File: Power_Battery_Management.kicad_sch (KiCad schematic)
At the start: 11 parts, among them J501 S2B-PH-SM4-TB, Q501 CSD85302L, U501 BQ29737, U502 MCP73831T-2ACI/MC

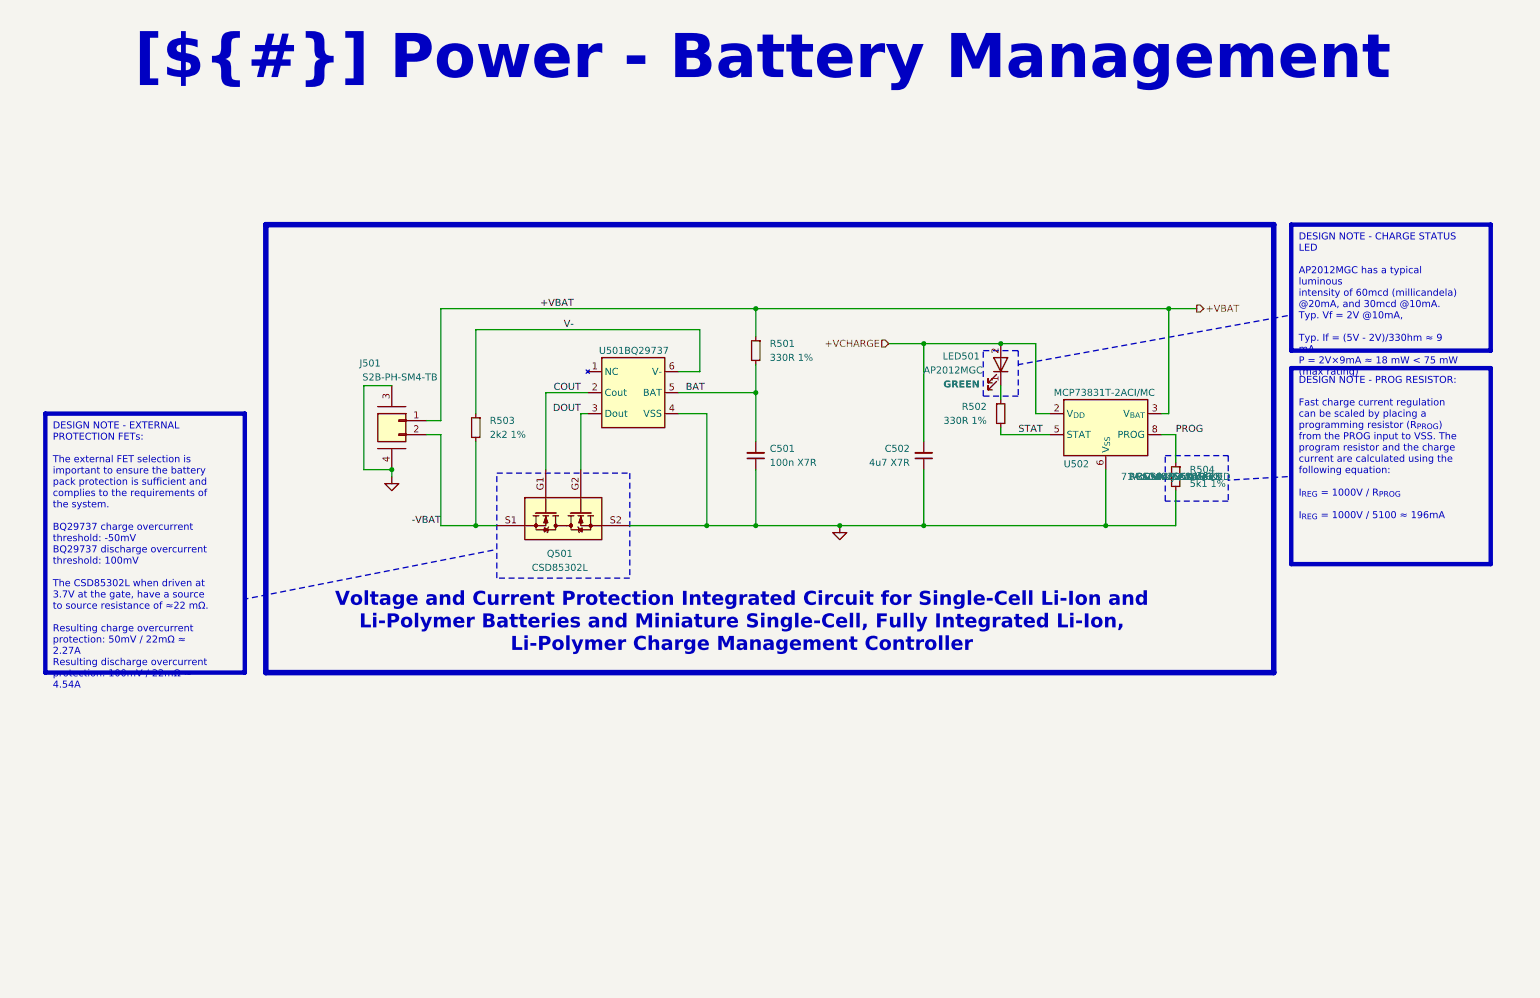
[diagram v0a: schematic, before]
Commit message: Added footprints, images, almost finished all èages except for the MCU
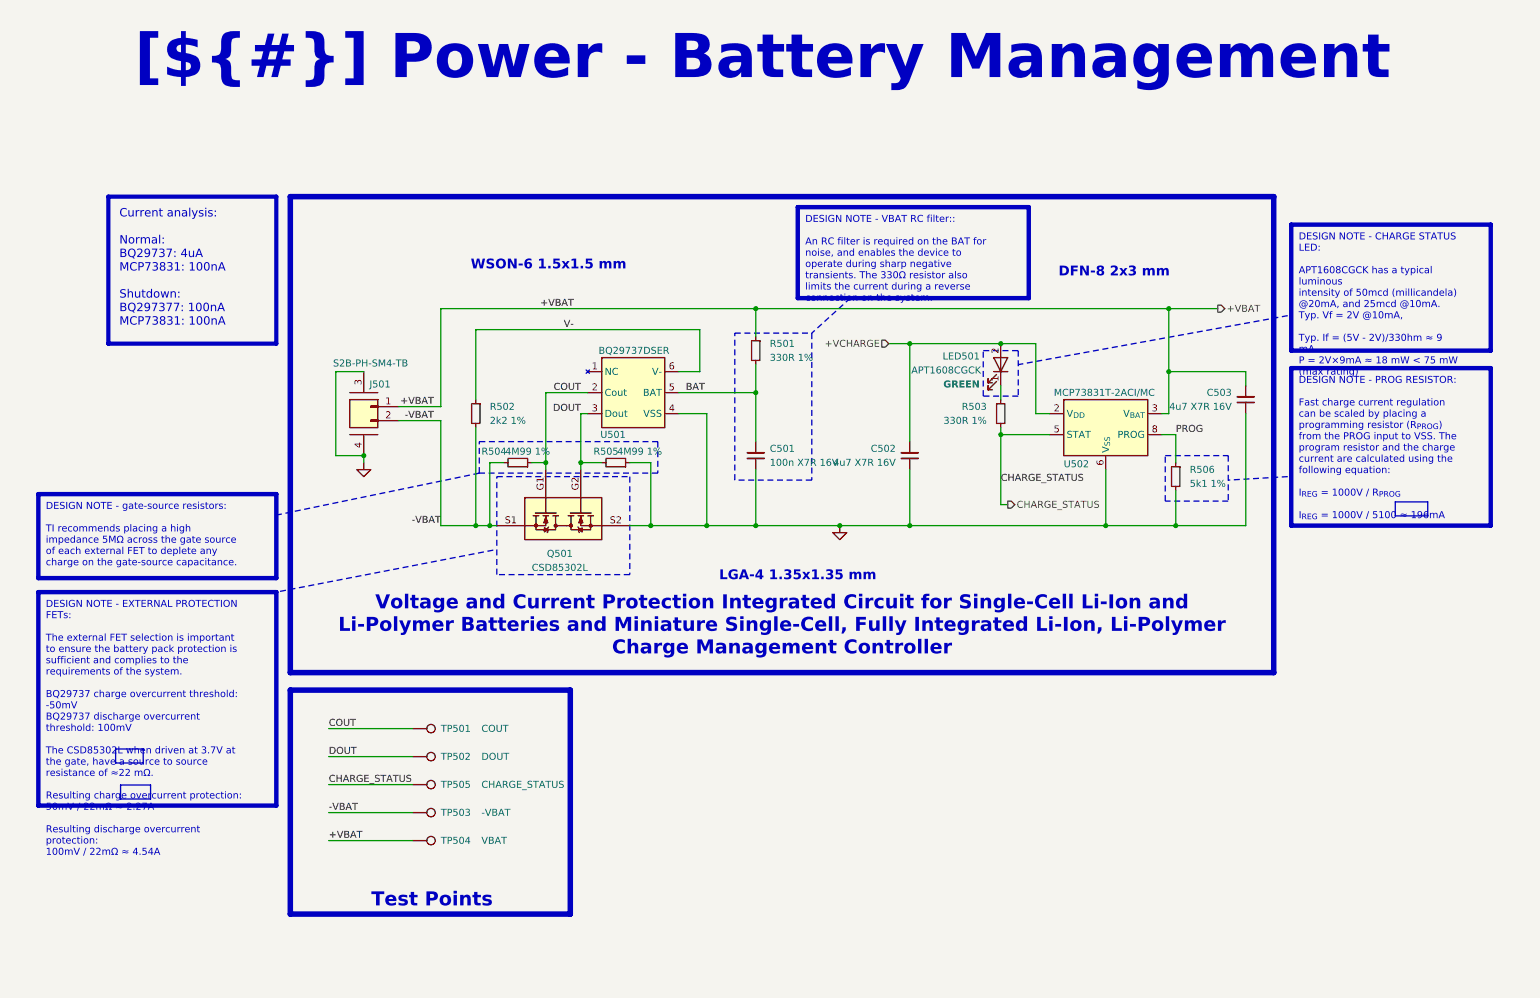
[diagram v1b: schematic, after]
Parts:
- removed J501: S2B-PH-SM4-TB, symbol 0_Plume:CONN_S2B-PH-SM4-TB_JST
- removed R502: 330R 1%, symbol Device:R_Small
- added C503: 4u7 X7R 16V, Capacitor_SMD:C_0603_1608Metric, symbol Device:C_Small
- added J501: S2B-PH-SM4-TB, 0_Plume:CONN_S2B-PH-SM4-TB_JST, symbol 0_connectors:Conn_01x02_Mounting
- added R503: 330R 1%, Resistor_SMD:R_0402_1005Metric, symbol Device:R_Small
- added R504, R505: 4M99 1%, Resistor_SMD:R_0402_1005Metric, symbol Device:R_Small
- added TP501: COUT, 0_Zenith:TestPoint_Pad_D0.5mm_Front, symbol Connector:TestPoint
- added TP502: DOUT, 0_Zenith:TestPoint_Pad_D0.5mm_Front, symbol Connector:TestPoint
- added TP503: -VBAT, 0_Zenith:TestPoint_Pad_D0.5mm_Front, symbol Connector:TestPoint
- added TP504: VBAT, 0_Zenith:TestPoint_Pad_D0.5mm_Front, symbol Connector:TestPoint
- added TP505: CHARGE_STATUS, 0_Zenith:TestPoint_Pad_D0.5mm_Front, symbol Connector:TestPoint
- C501: value 100n X7R -> 100n X7R 16V; footprint (none) -> Capacitor_SMD:C_0402_1005Metric; Manufacturer (none) -> Samsung Electro-Mechanics; Manufacturer Part Number (none) -> CL05B104KO5VPNC; Supplier (none) -> Mouser Electronics; Supplier Part Number (none) -> 187-CL05B104KO5VPNC
- C502: value 4u7 X7R -> 4u7 X7R 16V; footprint (none) -> Capacitor_SMD:C_0603_1608Metric; Manufacturer (none) -> Murata Electronics; Manufacturer Part Number (none) -> GRM188Z71C475KE21D; Supplier (none) -> Mouser Electronics; Supplier Part Number (none) -> 81-GRM188Z71C475KE1D
- LED501: footprint Charge_Manager_FP:KingBright_LED_0805 -> 0_Plume:KingBright_LED_0603; Manufacturer Part Number AP2012MGC -> APT1608CGCK; Supplier Part Number 604-AP2012MGC -> 604-APT1608CGCK
- Q501: footprint CSD85302L -> 0_Plume:CSD85302L; Manufacturer (none) -> Texas Instruments; Manufacturer Part Number (none) -> CSD85302L; Supplier (none) -> Mouser Electronics; Supplier Part Number (none) -> 595-CSD85302L
- R501: footprint (none) -> Resistor_SMD:R_0402_1005Metric; Manufacturer (none) -> KOA Speer; Manufacturer Part Number (none) -> RK73H1ETTP3300F; Supplier (none) -> Mouser Electronics; Supplier Part Number (none) -> 660-RK73H1ETTP3300F
- R502: renamed from R503; footprint (none) -> Resistor_SMD:R_0402_1005Metric; Manufacturer (none) -> KOA Speer; Manufacturer Part Number (none) -> RK73H1ETTP2201F; Supplier (none) -> Mouser Electronics; Supplier Part Number (none) -> 660-RK73H1ETTP2201F
- R506: renamed from R504; Manufacturer Vishay / Dale -> KOA Speer; Manufacturer Part Number RCS04025K10FKED -> RK73H1ETTP5101F; Supplier Part Number 71-RCS04025K10FKED -> 660-RK73H1ETTP5101F
- U501: value BQ29737 -> BQ29737DSER; Manufacturer (none) -> Texas Instruments; Manufacturer Part Number (none) -> BQ29737DSER; Supplier (none) -> Mouser Electronics; Supplier Part Number (none) -> 595-BQ29737DSER
- U502: footprint (none) -> 0_Plume:DFN_2x3mm; Manufacturer (none) -> Microchip Technology; Manufacturer Part Number (none) -> MCP73831T-2ACI/MC; Supplier (none) -> Mouser Electronics; Supplier Part Number (none) -> 579-MCP73831T-2ACIMC
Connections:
- net +VBAT: now also C503.2, J501.1 (Pin_1), TP504.1
- net -VBAT: now also J501.2 (Pin_2), R504.2, TP503.1
- net COUT: now also R504.1, TP501.1
- net DOUT: now also R505.2, TP502.1
- net GND: now also C503.1, J501.3 (MP1), J501.4 (MP2), R505.1
- net at LED501.1 (K): now also R503.1
- net STAT renamed CHARGE_STATUS
- net CHARGE_STATUS: now also R503.2, TP505.1
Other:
- note added: "DFN-8 2x3 mm"
- note added: "LGA-4 1.35x1.35 mm"
- note added: "WSON-6 1.5x1.5 mm"
- moved on the sheet: C502, R502

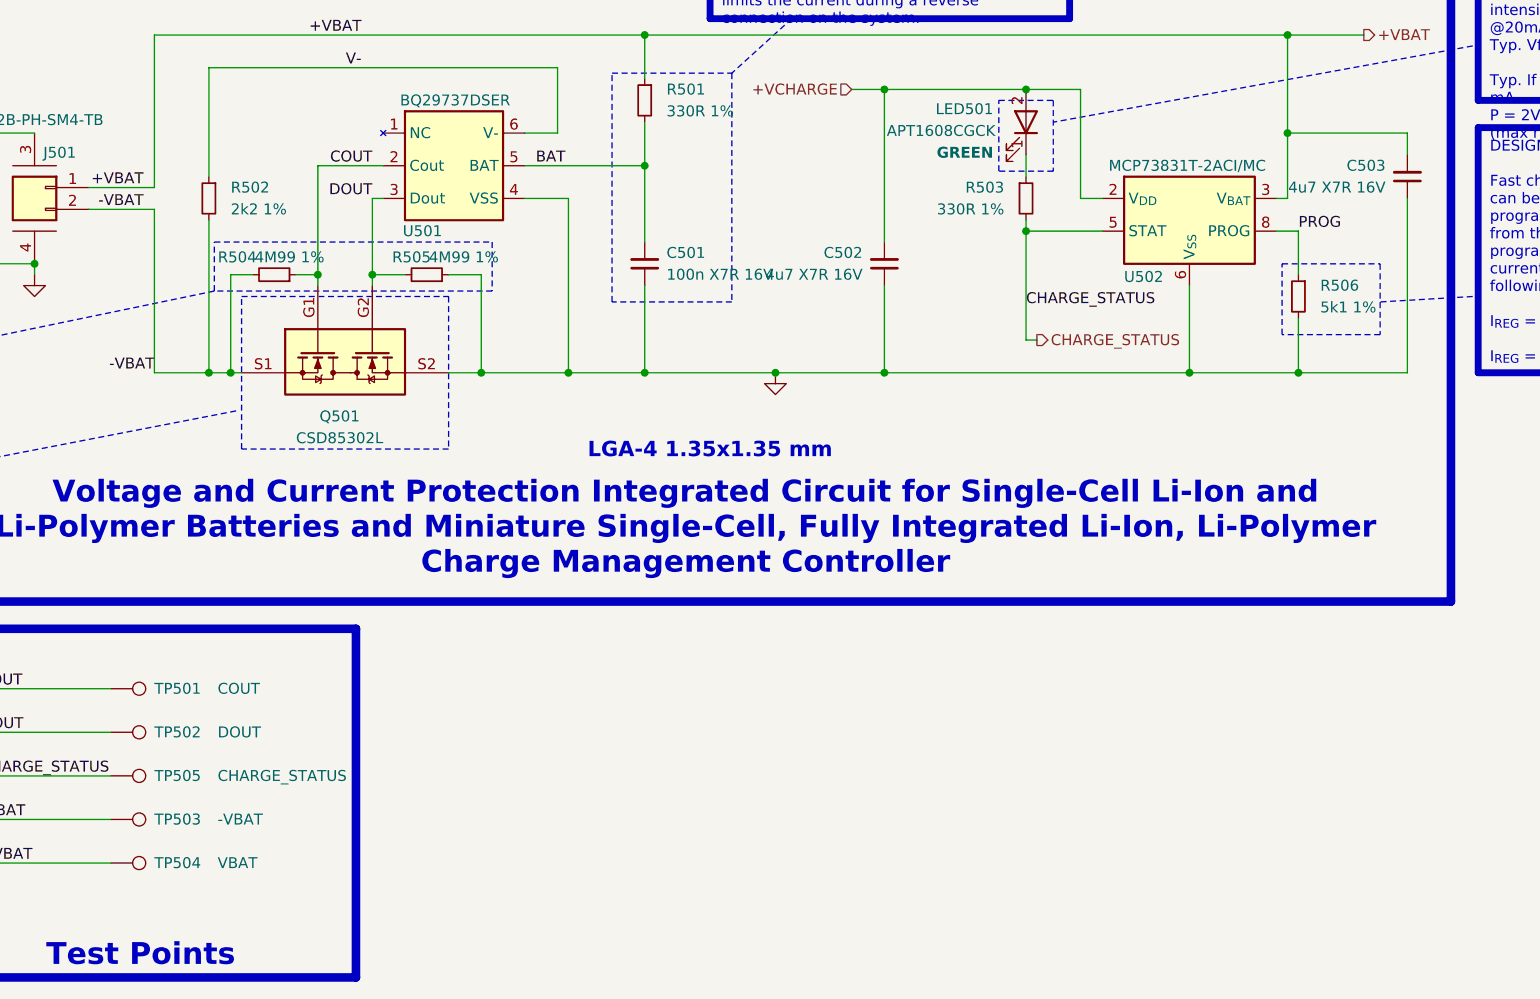
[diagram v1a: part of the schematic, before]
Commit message: Added RGB LED, added motor connectors, added test points, imported all 3D models
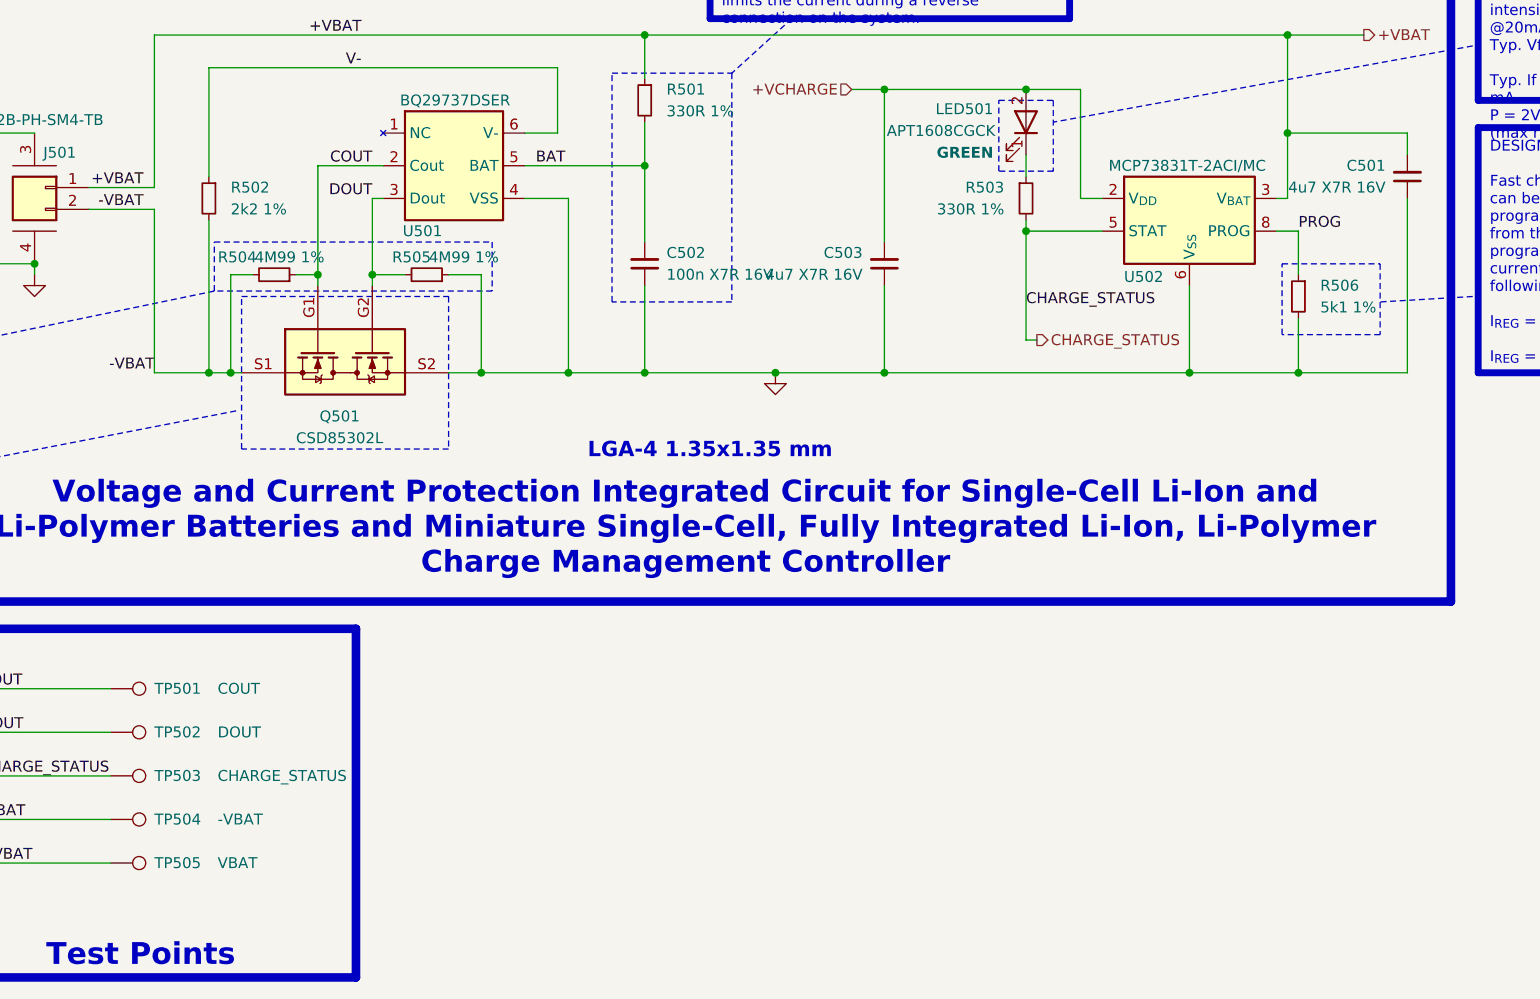
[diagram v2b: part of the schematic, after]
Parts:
- TP501, TP502: footprint 0_Zenith:TestPoint_Pad_D0.5mm_Front -> 0_Plume:TestPoint_Pad_D0.5mm_Back
- TP503: renamed from TP505; footprint 0_Zenith:TestPoint_Pad_D0.5mm_Front -> 0_Plume:TestPoint_Pad_D0.5mm_Back
- TP504: renamed from TP503; footprint 0_Zenith:TestPoint_Pad_D0.5mm_Front -> 0_Plume:TestPoint_Pad_D0.5mm_Back
- TP505: renamed from TP504; footprint 0_Zenith:TestPoint_Pad_D0.5mm_Front -> 0_Plume:TestPoint_Pad_D0.5mm_Back
- renumbered C503 to C501, C501 to C502, C502 to C503
